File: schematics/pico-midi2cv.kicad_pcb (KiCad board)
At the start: 2 copper layers, 75 x 55 mm, 33 parts, among them J1 Jack-DC (12-32V), U1 LM7805_TO220, U2 LM358, U3 MCP4822, U4 6N138

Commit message: Updated schematics
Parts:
- added D2: 1N4001, Zimo_Manual_PCB:D_Axial, F.Cu at (171.4, 56.1)
- R5: value 22k -> 100k
- R6: value 33k -> 51k
- moved J1 17.6 mm to (169.9, 67.6)
- moved R2 6.86 mm to (146.8, 71.1), turned to 0 degrees
- moved C1 6.12 mm to (170.7, 50.8), turned to 0 degrees
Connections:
- C1 pad 1: +12V -> Net-(C1-Pad1)
- C2 pad 1: +12V -> Net-(C1-Pad1)
- R2 pad 1: Net-(C5-Pad1) -> Net-(J_CV1-Pad1)
- U1 pad 1: +12V -> Net-(C1-Pad1)
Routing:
- net Net-(C1-Pad1): track 0.00 -> 20.7 mm
- net +12V: track 59.0 -> 40.9 mm
- net Net-(C5-Pad2): track 9.18 -> 20.5 mm
- net Net-(J_CV1-Pad1): track 4.55 -> 8.10 mm

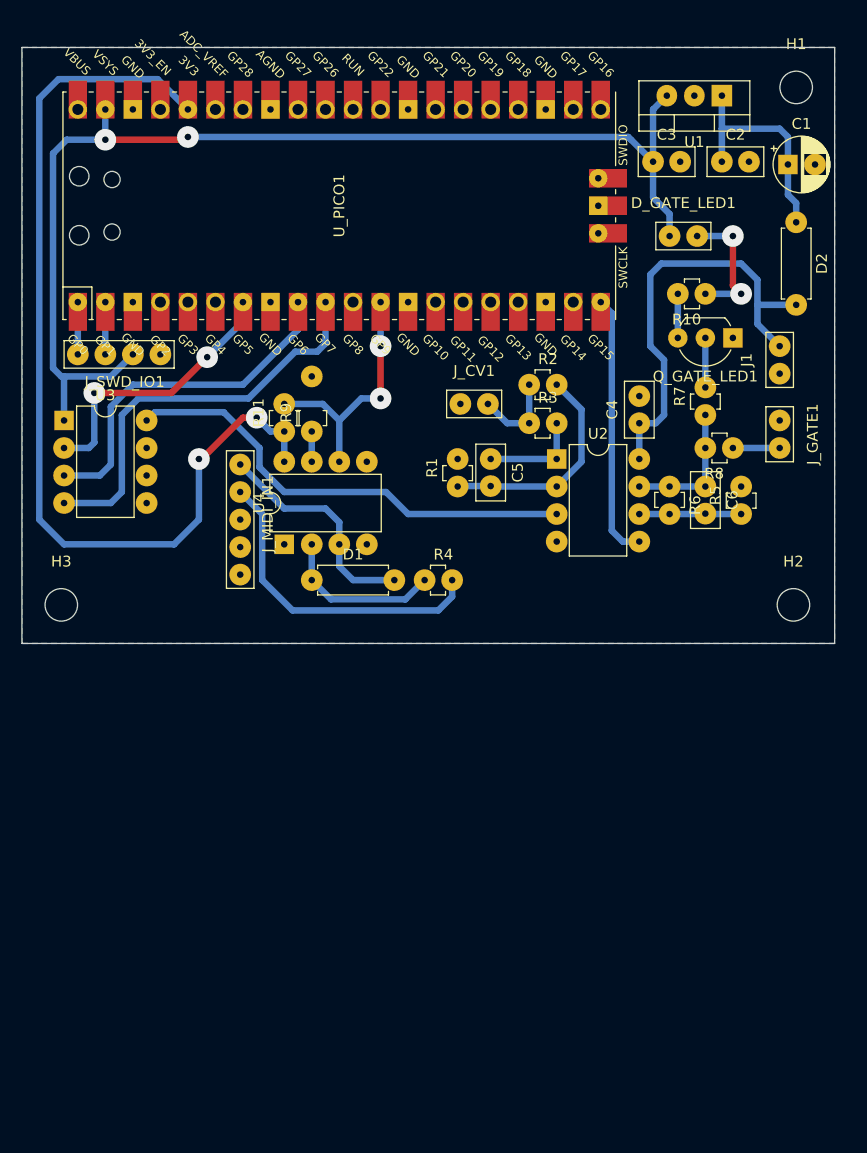
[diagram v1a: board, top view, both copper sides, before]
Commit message: Added MIDI channel DIP switch
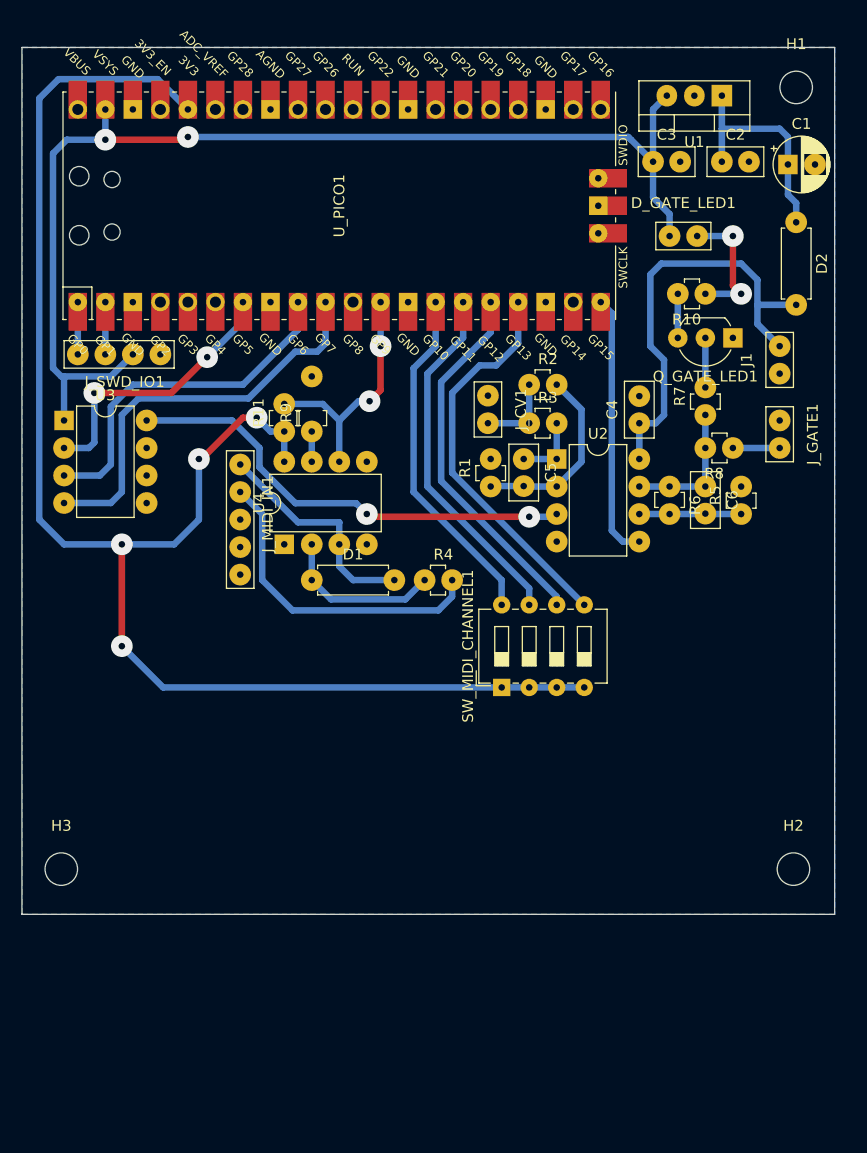
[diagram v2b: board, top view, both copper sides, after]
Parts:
- added SW_MIDI_CHANNEL1: SW_DIP_x04, Button_Switch_THT:SW_DIP_SPSTx04_Slide_6.7x11.72mm_W7.62mm_P2.54mm_LowProfile, F.Cu at (144.3, 99.1)
- moved H2 24.4 mm to (171.2, 115.8)
- moved H3 24.4 mm to (103.6, 115.8)
- moved C5 3.05 mm to (146.3, 78.0)
- moved R1 3.05 mm to (143.3, 80.5)
- moved J_CV1 1.78 mm to (143.0, 74.7), turned to 90 degrees
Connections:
- U_PICO1 pad 14: Net-(U_PICO1-Pad14) -> MIDI_CH_0
- U_PICO1 pad 15: Net-(U_PICO1-Pad15) -> MIDI_CH_1
- U_PICO1 pad 16: Net-(U_PICO1-Pad16) -> MIDI_CH_2
- U_PICO1 pad 17: Net-(U_PICO1-Pad17) -> MIDI_CH_3
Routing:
- net +3V3: track 89.5 -> 143.1 mm, vias 2 -> 4
- net MIDI_CH_3: track 0.00 -> 36.4 mm
- net MIDI_CH_2: track 0.00 -> 34.3 mm
- net MIDI_CH_1: track 0.00 -> 33.2 mm
- net MIDI_CH_0: track 0.00 -> 32.1 mm
- net Net-(C5-Pad1): track 9.40 -> 6.35 mm
- net Net-(C5-Pad2): track 20.5 -> 17.5 mm
- net Net-(J_CV1-Pad1): track 8.10 -> 7.37 mm
- net DAC_A: track 43.1 -> 42.7 mm, vias 0 -> 2
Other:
- board size 75 x 55 mm -> 75 x 80 mm

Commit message: Added top 20 pin outs to PCB and further updates
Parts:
- added J2: Conn_01x20_Male, Zimo_Manual_PCB:PinOut_01x20, F.Cu at (105.2, 45.0)
- added J3: Power 1, Zimo_Manual_PCB:NSL25_01x02_Vertical, F.Cu at (158.2, 58.4)
- added J4: Power 2, Zimo_Manual_PCB:NSL25_01x02_Vertical, F.Cu at (158.5, 102.9)
- added J5: Power to MCU, Zimo_Manual_PCB:PinOut_01x02, F.Cu at (159.5, 43.2)
- moved H2 9.65 mm to (171.2, 106.2)
- moved H3 9.65 mm to (103.6, 106.2)
- moved D_GATE_LED1 4.93 mm to (167.1, 58.4)
- moved C1 3.81 mm to (170.7, 54.6)
- moved C2 3.81 mm to (164.6, 54.4)
- moved C3 3.81 mm to (158.2, 54.4)
- moved C4 3.81 mm to (157.0, 78.5)
- moved C5 3.81 mm to (146.3, 81.8)
- moved C6 3.81 mm to (163.1, 84.3)
- moved D1 3.81 mm to (126.7, 93.0)
- moved D2 3.81 mm to (171.4, 59.9)
- moved J1 3.81 mm to (169.9, 71.4)
- moved J_CV1 3.81 mm to (143.0, 78.5)
- moved J_GATE1 3.81 mm to (169.9, 80.8)
- moved J_SWD_IO1 3.81 mm to (102.6, 72.1)
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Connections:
- net +3V3 renamed PB_HI
- net GND renamed PB_LO
- C3 pad 1: SWD_VSYS -> Net-(C3-Pad1)
- U1 pad 3: SWD_VSYS -> Net-(C3-Pad1)
- U_PICO1 pad 31: Net-(U_PICO1-Pad31) -> PB_VAL
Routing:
- net PB_HI: track 143.1 -> 160.1 mm, vias 4 -> 6
- net Net-(C3-Pad1): track 0.00 -> 11.7 mm
- net SWD_VSYS: track 106.3 -> 116.7 mm
- net +12V: track 40.9 -> 46.8 mm
- net PB_VAL: track 0.00 -> 4.57 mm
- net Net-(J2-Pad9): track 0.00 -> 4.57 mm
- net Net-(J2-Pad8): track 0.00 -> 4.57 mm
- net Net-(J2-Pad7): track 0.00 -> 4.57 mm
- net Net-(J2-Pad6): track 0.00 -> 4.57 mm
- net Net-(J2-Pad4): track 0.00 -> 4.57 mm
- net Net-(J2-Pad20): track 0.00 -> 4.57 mm
- net Net-(J2-Pad19): track 0.00 -> 4.57 mm
- net Net-(J2-Pad17): track 0.00 -> 4.57 mm
- net Net-(J2-Pad16): track 0.00 -> 4.57 mm
- net Net-(J2-Pad15): track 0.00 -> 4.57 mm
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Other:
- board size 75 x 80 mm -> 75 x 70 mm
- board text added: "This jumper must be disconnected when programming!!"

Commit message: Bugfixes
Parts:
- added J6: MIDI Keyboard Power, Zimo_Manual_PCB:NSL25_01x02_Vertical, F.Cu at (166.1, 102.9)
- moved H2 30.7 mm to (172.0, 136.9)
- moved H3 25.6 mm to (113.5, 129.8)
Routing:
- net +12V: track 46.8 -> 81.5 mm
- net GATE_OUT: track 24.5 -> 23.6 mm, vias 0 -> 2
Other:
- board size 75 x 70 mm -> 75 x 100 mm
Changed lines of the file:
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@@
   (general
     (thickness 1.6)
-    (drawings 7)
-    (tracks 218)
+    (drawings 8)
+    (tracks 229)
     (zones 0)
-    (modules 39)
+    (modules 40)
     (nets 61)
   )
@@
   )
   (module MountingHole:MountingHole_3mm (layer F.Cu)
-    (at 171.196 106.172)
+    (at 171.958 136.906)
     (descr "Mounting Hole 3mm, no annular")
     (tags "mounting hole 3mm no annular")
@@
   )
   (module MountingHole:MountingHole_3mm (layer F.Cu)
-    (at 103.632 106.172)
+    (at 113.538 129.794)
     (descr "Mounting Hole 3mm, no annular")
     (tags "mounting hole 3mm no annular")
@@
       (net 2 SWD_VSYS))
   )
+  (module Zimo_Manual_PCB:NSL25_01x02_Vertical (layer F.Cu)
+    (at 166.116 102.87)
+    (fp_text reference J6 (at 1.27 3.048) (layer F.SilkS)
+      (effects (font (size 1 1) (thickness 0.15)))
+    )
+    (fp_text value "MIDI Keyboard Power" (at 1.524 -4.064) (layer F.Fab)
+      (effects (font (size 1 1) (thickness 0.15)))
+    )
+    (fp_line (start 4.064 -2.54) (end -1.524 -2.54) (layer Dwgs.User) (width 0.12))
+    (fp_line (start 4.064 2.032) (end 4.064 -2.54) (layer Dwgs.User) (width 0.12))
+    (fp_line (start -1.524 2.032) (end 4.064 2.032) (layer Dwgs.User) (width 0.12))
+    (fp_line (start -1.524 -2.54) (end -1.524 2.032) (layer Dwgs.User) (width 0.12))
+    (fp_line (start -1.27 1.27) (end -1.27 -1.27) (layer F.SilkS) (width 0.12))
+    (fp_line (start 3.81 1.27) (end -1.27 1.27) (layer F.SilkS) (width 0.12))
+    (fp_line (start 3.81 -1.27) (end 3.81 1.27) (layer F.SilkS) (width 0.12))
+    (fp_line (start -1.27 -1.27) (end 3.81 -1.27) (layer F.SilkS) (width 0.12))
+    (pad 1 thru_hole circle (at 0 0) (size 2 2) (drill 0.6) (layers *.Cu *.Mask)
+      (net 1 +12V))
+    (pad 2 thru_hole circle (at 2.54 0) (size 2 2) (drill 0.6) (layers *.Cu *.Mask)
+      (net 43 PB_LO))
+  )
+  (dimension 100 (width 0.05) (layer F.CrtYd)
+    (gr_text "100.000 mm" (at 191.2 90 270) (layer F.CrtYd)
+      (effects (font (size 1 1) (thickness 0.15)))
+    )
+    (feature1 (pts (xy 175 140) (xy 190.586421 140)))
+    (feature2 (pts (xy 175 40) (xy 190.586421 40)))
+    (crossbar (pts (xy 190 40) (xy 190 140)))
+    (arrow1a (pts (xy 190 140) (xy 189.413579 138.873496)))
+    (arrow1b (pts (xy 190 140) (xy 190.586421 138.873496)))
+    (arrow2a (pts (xy 190 40) (xy 189.413579 41.126504)))
+    (arrow2b (pts (xy 190 40) (xy 190.586421 41.126504)))
+  )
   (gr_line (start 157.988 27.686) (end 157.988 41.402) (layer F.CrtYd) (width 0.05))
   (gr_text "This jumper must be disconnected when\nprogramming!!" (at 158.75 25.146) (layer F.CrtYd)
@@
     (arrow2b (pts (xy 100 30) (xy 101.126504 29.413579)))
   )
-  (gr_line (start 100 110) (end 100 40) (layer Edge.Cuts) (width 0.05))
-  (gr_line (start 175 110) (end 100 110) (layer Edge.Cuts) (width 0.05))
-  (gr_line (start 175 40) (end 175 110) (layer Edge.Cuts) (width 0.05))
+  (gr_line (start 100 140) (end 100 40) (layer Edge.Cuts) (width 0.05))
+  (gr_line (start 175 140) (end 100 140) (layer Edge.Cuts) (width 0.05))
+  (gr_line (start 175 40) (end 175 140) (layer Edge.Cuts) (width 0.05))
   (gr_line (start 100 40) (end 175 40) (layer Edge.Cuts) (width 0.05))
   (segment (start 156.972 81.788) (end 156.972 78.486) (width 0.6) (layer B.Cu) (net 1))
@@
   (segment (start 158.242 58.42) (end 158.242 64.008) (width 0.6) (layer B.Cu) (net 1))
   (segment (start 157.988 64.77) (end 158.496 64.262) (width 0.6) (layer B.Cu) (net 1))
+  (segment (start 163.83 94.488) (end 166.116 96.774) (width 0.6) (layer B.Cu) (net 1))
+  (segment (start 155.448 94.488) (end 163.83 94.488) (width 0.6) (layer B.Cu) (net 1))
+  (segment (start 166.116 96.774) (end 166.116 102.87) (width 0.6) (layer B.Cu) (net 1))
+  (segment (start 152.654 91.694) (end 155.448 94.488) (width 0.6) (layer B.Cu) (net 1))
+  (segment (start 156.972 81.788) (end 154.686 81.788) (width 0.6) (layer B.Cu) (net 1))
+  (segment (start 152.654 83.82) (end 152.654 91.694) (width 0.6) (layer B.Cu) (net 1))
+  (segment (start 154.686 81.788) (end 152.654 83.82) (width 0.6) (layer B.Cu) (net 1))
   (via (at 107.696 52.324) (size 2) (drill 0.6) (layers F.Cu B.Cu) (net 2))
   (segment (start 107.696 49.53) (end 107.696 52.324) (width 0.6) (layer B.Cu) (net 2))
@@
   (segment (start 146.812 87.122) (end 132.08 87.122) (width 0.6) (layer F.Cu) (net 20))
   (via (at 131.826 86.868) (size 2) (drill 0.6) (layers F.Cu B.Cu) (net 20))
-  (segment (start 154.432 88.392) (end 154.432 68.326) (width 0.6) (layer B.Cu) (net 21))
-  (segment (start 154.432 68.326) (end 153.416 67.31) (width 0.6) (layer B.Cu) (net 21))
-  (segment (start 155.448 89.408) (end 154.432 88.392) (width 0.6) (layer B.Cu) (net 21))
-  (segment (start 156.972 89.408) (end 155.448 89.408) (width 0.6) (layer B.Cu) (net 21))
+  (via (at 154.662 84.328) (size 2) (drill 0.6) (layers F.Cu B.Cu) (net 21))
+  (segment (start 154.662 87.098) (end 154.662 84.328) (width 0.6) (layer B.Cu) (net 21))
+  (segment (start 156.972 89.408) (end 154.662 87.098) (width 0.6) (layer B.Cu) (net 21))
+  (via (at 153.670002 78.994) (size 2) (drill 0.6) (layers F.Cu B.Cu) (net 21))
+  (segment (start 154.662 79.985998) (end 153.670002 78.994) (width 0.6) (layer F.Cu) (net 21))
+  (segment (start 154.662 84.328) (end 154.662 79.985998) (width 0.6) (layer F.Cu) (net 21))
+  (segment (start 153.416 67.31) (end 153.416 78.739998) (width 0.6) (layer B.Cu) (net 21))
+  (segment (start 153.416 78.739998) (end 153.670002 78.994) (width 0.6) (layer B.Cu) (net 21))
   (segment (start 125.222 71.882) (end 127.254 71.882) (width 0.6) (layer B.Cu) (net 22))
   (segment (start 128.016 71.12) (end 128.016 67.31) (width 0.6) (layer B.Cu) (net 22))
@@
     (polygon
       (pts
-        (xy 175 110) (xy 100 110) (xy 100 40) (xy 175 40)
+        (xy 175 140) (xy 100 140) (xy 100 40) (xy 175 40)
       )
     )

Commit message: Updated to KiCad7 format
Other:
- net class Default removed
